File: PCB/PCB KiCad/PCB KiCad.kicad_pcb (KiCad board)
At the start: 2 copper layers, 80 x 120 mm, 83 parts, among them J1 ADC Debug, J2 LED Debug, J3 Qwiic, SW1 MCU_RESET, SW2 TRIGGER, U1 OPA2376xxD, U2 ADS1256IDBT, U3 LM285D-2.5, U4 AMS1117-3.3, U5 TLC59208FIPWR, Y1 7.68MHz

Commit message: adds wavelengths to BOM
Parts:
- C15: value 10 -> 10u
- D10: value LED -> 1550nm
- D11: value LED -> 1650nm
- D4: value LED -> 855nm
- D5: value LED -> 940nm
- D6: value LED -> 1050nm
- D7: value LED -> 1200nm
- D8: value LED -> 1300nm
- D9: value LED -> 1460nm
- R17: value 150 -> 100
- R25: value 56 -> 52
- R26: value 62 -> 200
- R27: value 70 -> 150
- R28: value 75 -> 220
- R29: value 75 -> 240
- R30, R31: value 75 -> 150
- R32: value 82 -> 40
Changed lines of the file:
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@@
       (effects (font (size 1 1) (thickness 0.15)))
     )
-    (fp_text value "LED" (at 0 1.82 10) (layer "F.Fab")
+    (fp_text value "940nm" (at 0 1.82 10) (layer "F.Fab")
       (effects (font (size 1 1) (thickness 0.15)))
     )
@@
       (effects (font (size 1 1) (thickness 0.15)))
     )
-    (fp_text value "56" (at 0 1.65) (layer "F.Fab")
+    (fp_text value "52" (at 0 1.65) (layer "F.Fab")
       (effects (font (size 1 1) (thickness 0.15)))
     )
@@
       (effects (font (size 1 1) (thickness 0.15)))
     )
-    (fp_text value "70" (at 0 1.65) (layer "F.Fab")
+    (fp_text value "150" (at 0 1.65) (layer "F.Fab")
       (effects (font (size 1 1) (thickness 0.15)))
     )
@@
       (effects (font (size 1 1) (thickness 0.15)))
     )
-    (fp_text value "LED" (at 0 1.82 170) (layer "F.Fab")
+    (fp_text value "1550nm" (at 0 1.82 170) (layer "F.Fab")
       (effects (font (size 1 1) (thickness 0.15)))
     )
@@
       (effects (font (size 1 1) (thickness 0.15)))
     )
-    (fp_text value "75" (at 0 1.65) (layer "F.Fab")
+    (fp_text value "150" (at 0 1.65) (layer "F.Fab")
       (effects (font (size 1 1) (thickness 0.15)))
     )
@@
       (effects (font (size 1 1) (thickness 0.15)))
     )
-    (fp_text value "LED" (at 0 1.82 30) (layer "F.Fab")
+    (fp_text value "1460nm" (at 0 1.82 30) (layer "F.Fab")
       (effects (font (size 1 1) (thickness 0.15)))
     )
@@
       (effects (font (size 1 1) (thickness 0.15)))
     )
-    (fp_text value "62" (at 0 1.65) (layer "F.Fab")
+    (fp_text value "200" (at 0 1.65) (layer "F.Fab")
       (effects (font (size 1 1) (thickness 0.15)))
     )
@@
       (effects (font (size 1 1) (thickness 0.15)))
     )
-    (fp_text value "10" (at 0 1.68 90) (layer "F.Fab")
+    (fp_text value "10u" (at 0 1.68 90) (layer "F.Fab")
       (effects (font (size 1 1) (thickness 0.15)))
     )
@@
       (effects (font (size 1 1) (thickness 0.15)))
     )
-    (fp_text value "75" (at 0 1.65) (layer "F.Fab")
+    (fp_text value "240" (at 0 1.65) (layer "F.Fab")
       (effects (font (size 1 1) (thickness 0.15)))
     )
@@
       (effects (font (size 1 1) (thickness 0.15)))
     )
-    (fp_text value "LED" (at 0 1.82 150) (layer "F.Fab")
+    (fp_text value "1050nm" (at 0 1.82 150) (layer "F.Fab")
       (effects (font (size 1 1) (thickness 0.15)))
     )
@@
       (effects (font (size 1 1) (thickness 0.15)))
     )
-    (fp_text value "LED" (at 0 1.82 110) (layer "F.Fab")
+    (fp_text value "1200nm" (at 0 1.82 110) (layer "F.Fab")
       (effects (font (size 1 1) (thickness 0.15)))
     )
@@
       (effects (font (size 1 1) (thickness 0.15)))
     )
-    (fp_text value "75" (at 0 1.65) (layer "F.Fab")
+    (fp_text value "150" (at 0 1.65) (layer "F.Fab")
       (effects (font (size 1 1) (thickness 0.15)))
     )
@@
       (effects (font (size 1 1) (thickness 0.15)))
     )
-    (fp_text value "LED" (at 0 1.82 50) (layer "F.Fab")
+    (fp_text value "855nm" (at 0 1.82 50) (layer "F.Fab")
       (effects (font (size 1 1) (thickness 0.15)))
     )
@@
       (effects (font (size 1 1) (thickness 0.15)))
     )
-    (fp_text value "82" (at 0 1.65) (layer "F.Fab")
+    (fp_text value "40" (at 0 1.65) (layer "F.Fab")
       (effects (font (size 1 1) (thickness 0.15)))
     )
@@
       (effects (font (size 1 1) (thickness 0.15)))
     )
-    (fp_text value "LED" (at 0 1.82 130) (layer "F.Fab")
+    (fp_text value "1650nm" (at 0 1.82 130) (layer "F.Fab")
       (effects (font (size 1 1) (thickness 0.15)))
     )
@@
       (effects (font (size 1 1) (thickness 0.15)))
     )
-    (fp_text value "LED" (at 0 1.82 70) (layer "F.Fab")
+    (fp_text value "1300nm" (at 0 1.82 70) (layer "F.Fab")
       (effects (font (size 1 1) (thickness 0.15)))
     )
@@
       (effects (font (size 1 1) (thickness 0.15)))
     )
-    (fp_text value "75" (at 0 1.65) (layer "F.Fab")
+    (fp_text value "220" (at 0 1.65) (layer "F.Fab")
       (effects (font (size 1 1) (thickness 0.15)))
     )
@@
       (effects (font (size 1 1) (thickness 0.15)))
     )
-    (fp_text value "150" (at 0 1.65 90) (layer "F.Fab")
+    (fp_text value "100" (at 0 1.65 90) (layer "F.Fab")
       (effects (font (size 1 1) (thickness 0.15)))
     )

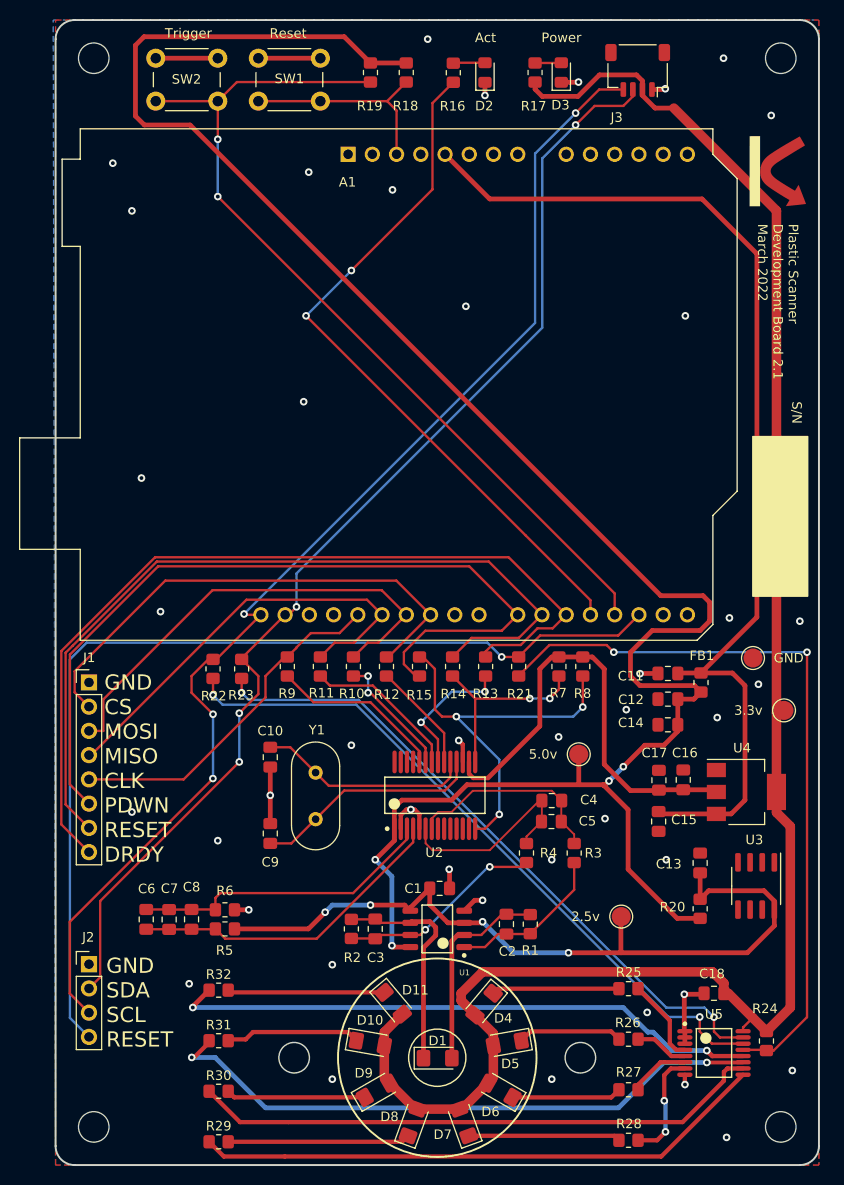
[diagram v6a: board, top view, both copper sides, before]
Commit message: v2.2.0 first attempt for new ICs
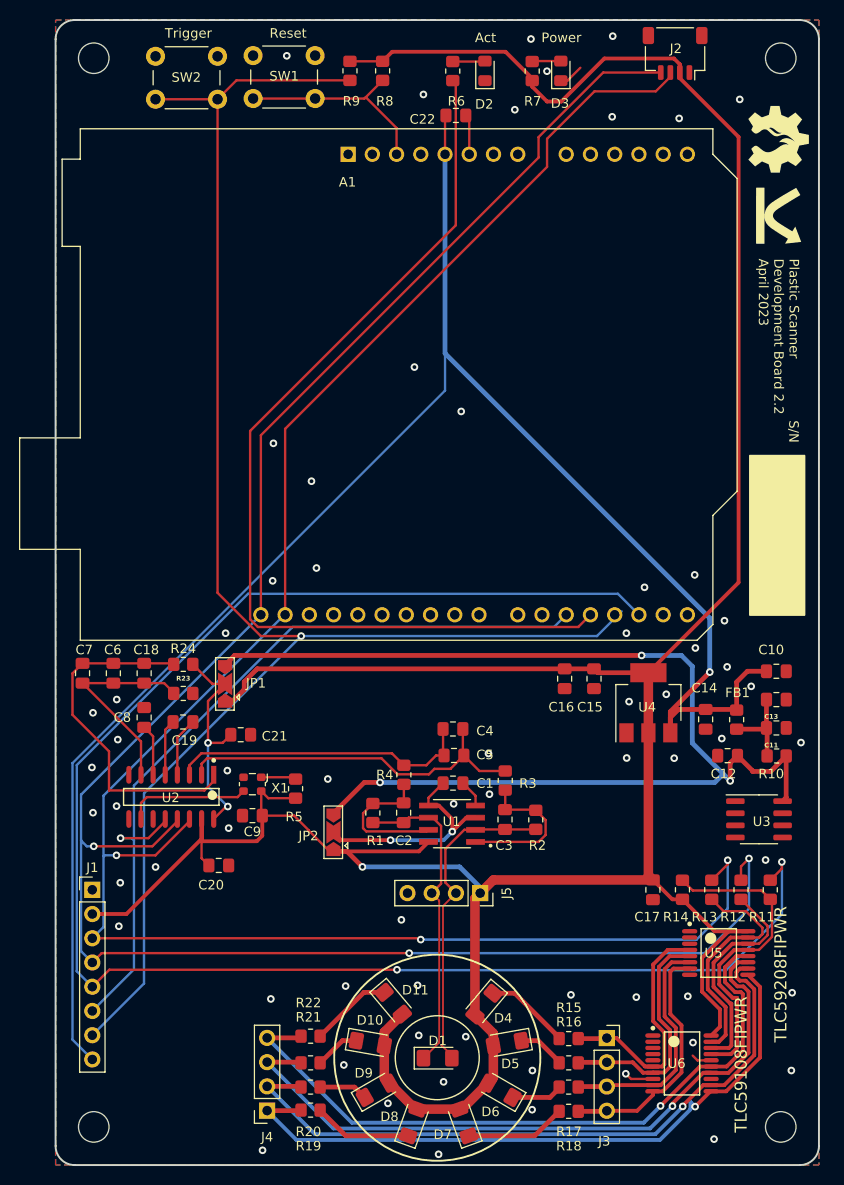
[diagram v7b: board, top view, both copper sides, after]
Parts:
- removed 2.5v, 3.3v, 5.0v, GND: TestPoint_Pad_D2.0mm, TestPoint:TestPoint_Pad_D2.0mm
- removed the J2 at (46.5, 127.0)
- removed the R15 at (81.1, 95.8)
- removed the R16 at (84.7, 33.5)
- removed the R17 at (93.2, 33.5)
- removed the R18 at (79.8, 33.5)
- removed the R19 at (76.0, 33.5)
- removed the R20 at (110.5, 121.1)
- removed the R21 at (91.5, 95.8)
- removed the R22 at (59.5, 96.0)
- removed the REF** at (119.0, 43.8)
- removed Y1: 7.68MHz, Crystal:Crystal_HC49-U_Vertical
- added C19: 330u, Capacitor_SMD:C_0805_2012Metric_Pad1.18x1.45mm_HandSolder, F.Cu at (56.4, 101.6)
- added C20: 0.1u, Capacitor_SMD:C_0805_2012Metric_Pad1.18x1.45mm_HandSolder, F.Cu at (60.1, 116.6)
- added C21: 0.1u, Capacitor_SMD:C_0805_2012Metric_Pad1.18x1.45mm_HandSolder, F.Cu at (62.4, 102.9)
- added C22: 0.1u, Capacitor_SMD:C_0805_2012Metric_Pad1.18x1.45mm_HandSolder, F.Cu at (85.0, 38.0)
- added G***: LOGO, LOGO, F.Cu at (119.0, 48.5)
- added G***: LOGO, LOGO, F.Cu at (118.8, 40.5)
- added G***: LOGO, LOGO, B.Cu at (84.8, 105.1)
- added G1: LOGO, LOGO, B.Cu at (82.0, 66.0)
- added J3: Conn_01x04, Connector_PinSocket_2.54mm:PinSocket_1x04_P2.54mm_Vertical, F.Cu at (100.8, 134.7)
- added J4: Conn_01x04, Connector_PinSocket_2.54mm:PinSocket_1x04_P2.54mm_Vertical, F.Cu at (65.2, 142.3)
- added J5: Conn_01x04, Connector_PinSocket_2.54mm:PinSocket_1x04_P2.54mm_Vertical, F.Cu at (87.5, 119.5)
- added JP1: SolderJumper_3_Open, Jumper:SolderJumper-3_P2.0mm_Open_TrianglePad1.0x1.5mm, F.Cu at (60.8, 97.6)
- added JP2: SolderJumper_3_Open, Jumper:SolderJumper-3_P2.0mm_Open_TrianglePad1.0x1.5mm, F.Cu at (72.1, 113.1)
- added U6: TLC59108FIPWR, TLC59108:Texas_Instruments-TLC59108FIPWR-Level_A, F.Cu at (108.6, 137.3)
- added X1: 4.9152 MHz, Oscillator:Oscillator_SMD_ECS_2520MV-xxx-xx-4Pin_2.5x2.0mm, F.Cu at (63.6, 108.1)
- C1: value 100n -> 0.1u
- C10: value 18p -> 10u
- C11: value 10u -> 22u
- C12, C17: value 22u -> 100n
- C14: value 100n -> 10u
- C15: value 10u -> 100n
- C16, C18: value 100n -> 22u
- C6: value 22u -> 0.1u
- C7: value 100n -> 100p
- C8: value 100p -> 0.1u
- C9: value 18p -> 0.1u
- D10: value 1550nm -> 1650nm
- D11: value 1650nm -> 1720nm
- D4: value 855nm -> 940nm
- D5: value 940nm -> 1050nm
- D6: value 1050nm -> 1200nm
- D7: value 1200nm -> 1300nm
- D8: value 1300nm -> 1460nm
- D9: value 1460nm -> 1550nm
- J1: value ADC Debug -> Conn_01x08
- R10, R14: value 100 -> 1k
- R12: value 100 -> 0
- R15: renamed from R25; value 52 -> 47
- R16: renamed from R26; value 200 -> 47
- R17: renamed from R27; value 150 -> 47
- R18: renamed from R28; value 220 -> 47
- R19: renamed from R29; value 240 -> 47
- R20: renamed from R30; value 150 -> 47
- R21: renamed from R31; value 150 -> 47
- R22: renamed from R32; value 40 -> 47
- R23: value 0 -> 49.9
- R24: value 1k -> 49.9
- R5: value 49.9 -> 1k
- R6: value 49.9 -> 100
- R7: value 10k -> 100
- R9: value 100 -> 10k
- U1: value OPA2376xxD -> OPA2376AID; footprint eec:Texas_Instruments-OPA2376AID-Level_A -> OPA2376AID:SOIC127P599X175-8N
- U2: value ADS1256IDBT -> NAU7802SGI; footprint ADS1256:Texas_Instruments-ADS1256IDBT-Level_A -> IC_Nuvoton_NAU7802SGI:Nuvoton-NAU7802SGI-0-0-0
- moved R6 91.1 mm to (84.6, 33.3), turned to 90 degrees
- moved R24 72.8 mm to (56.4, 95.5), turned to 0 degrees
- moved C18 68.5 mm to (52.3, 96.5), turned to 90 degrees
- moved R8 65.9 mm to (77.3, 33.3)
- moved R9 62.8 mm to (73.8, 33.3)
- moved R7 62.5 mm to (93.0, 33.3)
- moved C10 53.8 mm to (118.5, 96.2), turned to 0 degrees
- moved R11 52.6 mm to (117.9, 119.2)
- moved R10 45.3 mm to (118.6, 105.1), turned to 0 degrees
- moved R12 43.9 mm to (114.8, 119.2)
- moved R14 33.6 mm to (108.7, 119.2)
- moved R13 33.3 mm to (111.8, 119.2)
- moved U2 27.6 mm to (55.1, 109.4), turned to -90 degrees
- moved C7 27.4 mm to (45.8, 96.5)
- moved C6 26.0 mm to (49.1, 96.5)
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- renumbered J3 to J2
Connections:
- net Net-(R25-Pad1) renamed LED1
- net Net-(R26-Pad1) renamed LED2
- net Net-(R27-Pad1) renamed LED3
- net Net-(R28-Pad1) renamed LED4
- net Net-(R29-Pad1) renamed LED5
- net Net-(R30-Pad1) renamed LED6
- net Net-(R31-Pad1) renamed LED7
- net Net-(R32-Pad1) renamed LED8
- A1 pad 17: /LED/LED RESET -> LED_RESET
- A1 pad 18: /MCU + IO/TRIGGER -> TRIGGER
- A1 pad 19: /MCU + IO/LED BLUE -> LED_BLUE
- A1 pad 20: /ADC/ADC DRDY -> DRDY_INT
- A1 pad 21: /ADC/ADC RESET -> unconnected-(A1-D6-Pad21)
- A1 pad 22: /ADC/ADC PDWN -> unconnected-(A1-D7-Pad22)
- A1 pad 25: /ADC/SPI.CS -> unconnected-(A1-D10-Pad25)
- A1 pad 26: /ADC/SPI.MOSI -> unconnected-(A1-D11-Pad26)
- A1 pad 27: /ADC/SPI.MISO -> unconnected-(A1-D12-Pad27)
- A1 pad 28: /ADC/SPI.CLK -> unconnected-(A1-D13-Pad28)
- A1 pad 3: /MCU + IO/MCU RESET -> MCU_RESET
- A1 pad 31: /LED/I2C.SDA -> SDA
- A1 pad 32: /LED/I2C.SCL -> SCL
- A1 pad 5: /MCU + IO/+5V RAW -> 5v_RAW
- C1 pad 2: +2V5 -> Net-(JP2-C)
- C10 pad 1: Net-(C10-Pad1) -> 5v_RAW
- C11 pad 1: /MCU + IO/+5V RAW -> +5V
- C12 pad 1: +5V -> +2V5
- C13 pad 1: +2V5 -> +5V
- C14 pad 1: +5V -> 5v_RAW
- C15 pad 1: /MCU + IO/+5V RAW -> GND
- C15 pad 2: GND -> 3.3v
- C16 pad 1: GND -> 3.3v
- C16 pad 2: +3V3 -> GND
- C17 pad 1: +3V3 -> 3.3v
- C18 pad 1: +3V3 -> Net-(U2-REFN)
- C18 pad 2: GND -> Net-(U2-REFP)
- C2 pad 1: Net-(C2-Pad1) -> /Sensor/A-
- C2 pad 2: Net-(C2-Pad2) -> Net-(U1-OUT_B)
- C3 pad 1: Net-(C3-Pad1) -> /Sensor/A+
- C3 pad 2: Net-(C3-Pad2) -> Net-(U1-OUT_A)
- C6 pad 1: Net-(C6-Pad1) -> Net-(U2-REFN)
- C6 pad 2: Net-(C6-Pad2) -> Net-(U2-REFP)
- C7 pad 1: Net-(C6-Pad1) -> Net-(U2-REFN)
- C7 pad 2: Net-(C6-Pad2) -> Net-(U2-REFP)
- C8 pad 1: Net-(C6-Pad1) -> GND
- C8 pad 2: Net-(C6-Pad2) -> Net-(U2-VBG)
- C9 pad 1: GND -> 3.3v
- C9 pad 2: Net-(C9-Pad2) -> GND
- D1 pad 1: Net-(C3-Pad1) -> /Sensor/A-
- D1 pad 2: Net-(C2-Pad1) -> /Sensor/A+
- D10 pad 2: +3V3 -> 3.3v
- D11 pad 2: +3V3 -> 3.3v
- D2 pad 2: Net-(D2-Pad2) -> Net-(D2-A)
- D3 pad 2: Net-(D3-Pad2) -> Net-(D3-A)
- D4 pad 2: +3V3 -> 3.3v
- D5 pad 2: +3V3 -> 3.3v
- D6 pad 2: +3V3 -> 3.3v
- D7 pad 2: +3V3 -> 3.3v
- D8 pad 2: +3V3 -> 3.3v
- D9 pad 2: +3V3 -> 3.3v
- FB1 pad 2: /MCU + IO/+5V RAW -> 5v_RAW
- J1 pad 2: /ADC/SPI.CS -> 3.3v
- J1 pad 3: /ADC/SPI.MOSI -> SDA
- J1 pad 4: /ADC/SPI.MISO -> SCL
- J1 pad 5: /ADC/SPI.CLK -> LED_RESET
- J1 pad 6: /ADC/ADC PDWN -> DRDY_INT
- J1 pad 7: /ADC/ADC RESET -> TRIGGER
- J1 pad 8: /ADC/ADC DRDY -> 5v_RAW
- J2 pad 2: +3V3 -> 3.3v
- J2 pad 3: /LED/I2C.SDA -> SDA
- J2 pad 4: /LED/I2C.SCL -> SCL
- R1 pad 1: Net-(C2-Pad1) -> Net-(U1-OUT_B)
- R1 pad 2: Net-(C2-Pad2) -> /Sensor/A-
- R10 pad 1: /ADC/SPI.MOSI -> +5V
- R10 pad 2: Net-(R10-Pad2) -> +2V5
- R11 pad 1: /ADC/SPI.MISO -> LED_RESET
- R11 pad 2: Net-(R11-Pad2) -> Net-(U5-~{RESET})
- R12 pad 1: /ADC/SPI.CS -> SCL
- R12 pad 2: Net-(R12-Pad2) -> Net-(U5-SCL)
- R13 pad 1: /ADC/ADC DRDY -> SDA
- R13 pad 2: Net-(R13-Pad2) -> Net-(U5-SDA)
- R14 pad 1: /ADC/ADC RESET -> Net-(U5-~{RESET})
- R14 pad 2: Net-(R14-Pad2) -> 3.3v
- R2 pad 1: Net-(C3-Pad2) -> /Sensor/A+
- R2 pad 2: Net-(C3-Pad1) -> Net-(U1-OUT_A)
- R23 pad 1: /LED/I2C.SDA -> Net-(U2-REFN)
- R23 pad 2: Net-(R23-Pad2) -> GND
- R24 pad 1: Net-(R21-Pad2) -> Net-(U2-REFP)
- R24 pad 2: +3V3 -> Net-(JP1-C)
- R3 pad 1: Net-(C2-Pad2) -> Net-(U1-OUT_A)
- R4 pad 1: Net-(C3-Pad2) -> Net-(U1-OUT_B)
- R5 pad 1: +2V5 -> Net-(X1-Tri-State)
- R5 pad 2: Net-(C6-Pad1) -> 3.3v
- R6 pad 1: GND -> LED_BLUE
- R6 pad 2: Net-(C6-Pad2) -> Net-(D2-A)
- R7 pad 1: Net-(R14-Pad2) -> 3.3v
- R7 pad 2: +3V3 -> Net-(D3-A)
- R8 pad 1: +3V3 -> 3.3v
- R8 pad 2: Net-(R15-Pad2) -> MCU_RESET
- R9 pad 1: /ADC/SPI.CLK -> 3.3v
- R9 pad 2: Net-(R9-Pad2) -> TRIGGER
- SW1 pad 2: /MCU + IO/MCU RESET -> MCU_RESET
- SW2 pad 2: /MCU + IO/TRIGGER -> TRIGGER
- U1 pad 1: Net-(C2-Pad2) -> Net-(U1-OUT_A)
- U1 pad 2: Net-(C2-Pad1) -> /Sensor/A+
- U1 pad 3: +2V5 -> Net-(JP2-C)
- U1 pad 5: +2V5 -> Net-(JP2-C)
- U1 pad 6: Net-(C3-Pad1) -> /Sensor/A-
- U1 pad 7: Net-(C3-Pad2) -> Net-(U1-OUT_B)
- U1 pad 8: +5V -> 3.3v
- U2 pad 1: +5V -> Net-(U2-REFP)
- U2 pad 10: unconnected-(U2-Pad10) -> Net-(U2-XIN)
- U2 pad 12: unconnected-(U2-Pad12) -> DRDY_INT
- U2 pad 13: unconnected-(U2-Pad13) -> SCL
- U2 pad 14: Net-(R15-Pad2) -> SDA
- U2 pad 15: Net-(R14-Pad2) -> 3.3v
- U2 pad 16: +3V3 -> Net-(JP1-C)
- U2 pad 2: GND -> /ADC/AIN-
- U2 pad 3: Net-(C6-Pad2) -> /ADC/AIN+
- U2 pad 4: Net-(C6-Pad1) -> Net-(U2-VIN2N)
- U2 pad 5: GND -> Net-(U2-VIN2P)
- U2 pad 6: /ADC/AIN+ -> Net-(U2-VBG)
- U2 pad 7: /ADC/AIN- -> Net-(U2-REFN)
- U2 pad 8: unconnected-(U2-Pad8) -> GND
- U2 pad 9: unconnected-(U2-Pad9) -> GND
- U4 pad 2: +3V3 -> 3.3v
- U4 pad 3: /MCU + IO/+5V RAW -> 5v_RAW
- U5 pad 1: GND -> unconnected-(U5-A0-Pad1)
- U5 pad 13: Net-(R21-Pad2) -> Net-(U5-~{RESET})
- U5 pad 14: Net-(R22-Pad2) -> Net-(U5-SCL)
- U5 pad 15: Net-(R23-Pad2) -> Net-(U5-SDA)
- U5 pad 16: +3V3 -> 3.3v
- U5 pad 2: GND -> unconnected-(U5-A1-Pad2)
- U5 pad 3: GND -> unconnected-(U5-A2-Pad3)
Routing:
- net 3.3v: track 0.00 -> 342.6 mm, vias 0 -> 1
- net +3V3: track 240.5 -> 0.00 mm
- net SCL: track 0.00 -> 213.2 mm, vias 0 -> 3
- net +5V: track 220.7 -> 9.11 mm, vias 4 -> 0
- net SDA: track 0.00 -> 206.2 mm, vias 0 -> 3
- net 5v_RAW: track 0.00 -> 205.4 mm, vias 0 -> 1
- net LED_RESET: track 0.00 -> 174.5 mm, vias 0 -> 2
- net TRIGGER: track 0.00 -> 169.1 mm, vias 0 -> 1
- net /LED/I2C.SCL: track 127.9 -> 0.00 mm, vias 4 -> 0
- net /LED/I2C.SDA: track 121.2 -> 0.00 mm, vias 4 -> 0
- net /MCU + IO/+5V RAW: track 112.7 -> 0.00 mm
- net /LED/LED RESET: track 103.2 -> 0.00 mm, vias 1 -> 0
- net LED_BLUE: track 0.00 -> 102.0 mm
- net /MCU + IO/TRIGGER: track 94.4 -> 0.00 mm, vias 2 -> 0
- net /ADC/ADC DRDY: track 92.3 -> 0.00 mm
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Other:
- outline, holes or cut-outs redrawn
- board text added: "Plastic Scanner Development Board 2.2 April 2023"
- board text removed: "GND CS MOSI MISO CLK PDWN RESET DRDY"
- board text removed: "GND SDA SCL RESET"
- board text removed: "Plastic Scanner Development Board 2.1 March 2022"

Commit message: update pcb
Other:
- board text added: "GND 3.3V SDA SCL LED RST DRDY TRIG 5V raw"
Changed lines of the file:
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@@
     (effects (font (size 1 1) (thickness 0.15)))
+  )
+  (gr_text "GND\n3.3V\nSDA\nSCL\nLED RST\nDRDY\nTRIG\n5V raw" (at 48.75 138.15) (layer "F.SilkS")
+    (effects (font (size 1.55 1.5) (thickness 0.1875)) (justify left bottom))
   )
   (gr_text "Reset" (at 67.37 29.39) (layer "F.SilkS")
